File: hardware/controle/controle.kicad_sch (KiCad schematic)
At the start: 44 parts, among them J3 PWR, J4 DATA, J5 UART7, J6 TWI3, J7 SENS0375, J8 TWI4, J9 LED, U2 MCP7940N-xSN, U4 ULN2003, Y1 32.768Khz

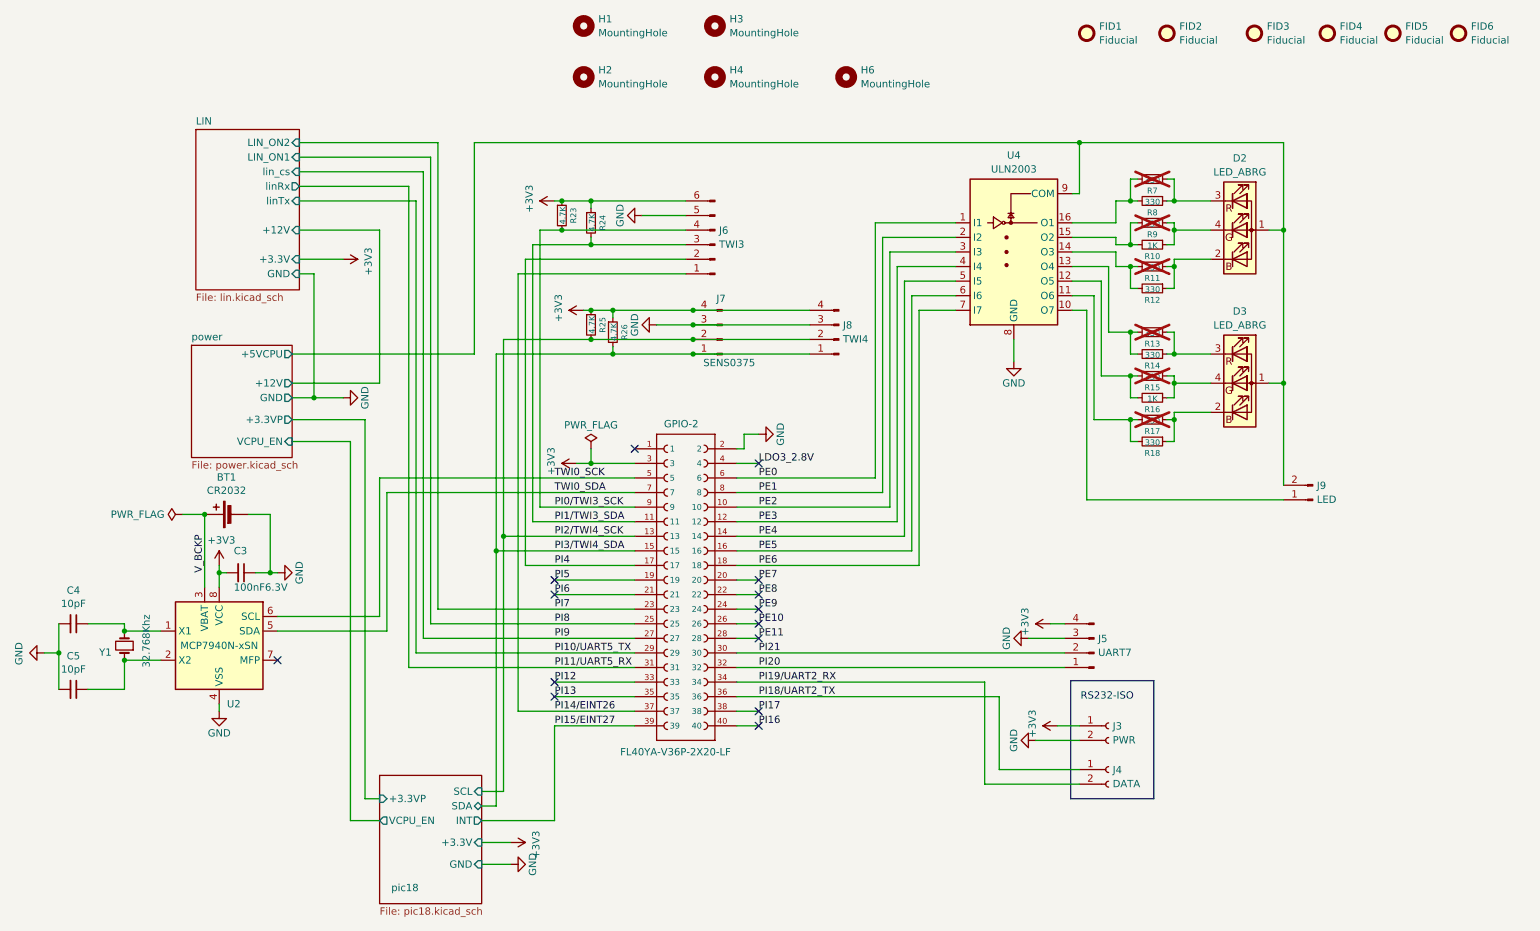
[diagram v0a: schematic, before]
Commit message: hardware/controle: route control CPU power from pic18
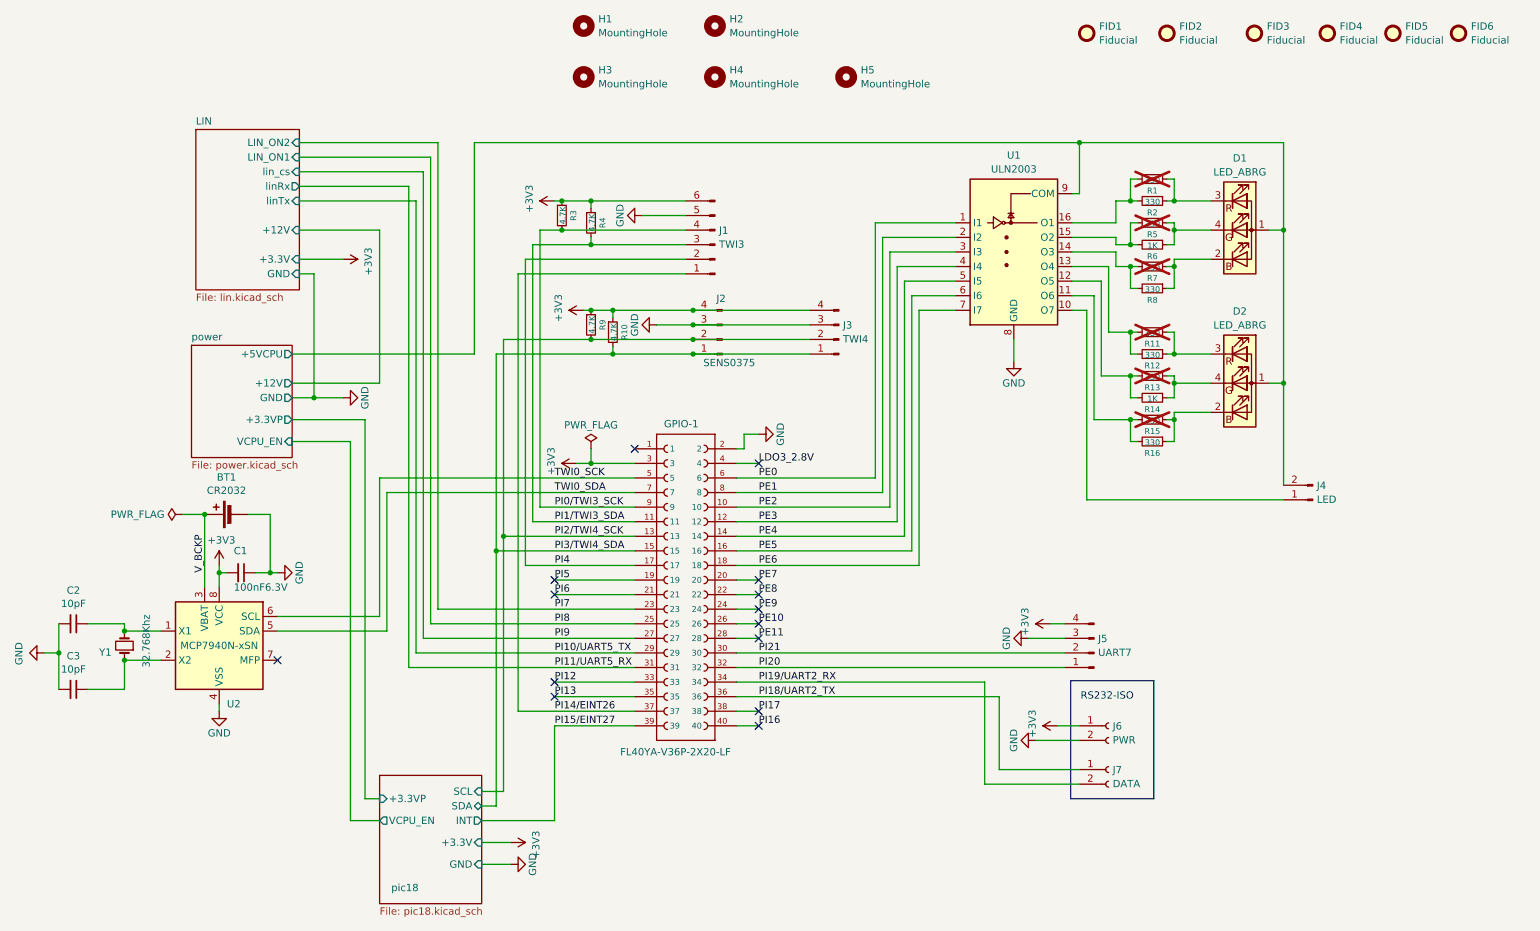
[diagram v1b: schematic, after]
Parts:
- renumbered C3 to C1, C4 to C2, C5 to C3, D2 to D1, D3 to D2, GPIO-2 to GPIO-1, H3 to H2, H2 to H3, H6 to H5, J6 to J1, J7 to J2, J8 to J3, J9 to J4, J3 to J6, J4 to J7, R7 to R1, R26 to R10, R13 to R11, R14 to R12, R15 to R13, R16 to R14, R17 to R15, R18 to R16, R8 to R2, R23 to R3, R24 to R4, R9 to R5, R10 to R6, R11 to R7, R12 to R8, R25 to R9, U4 to U1

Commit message: hardware/controle: update some component values and P/N
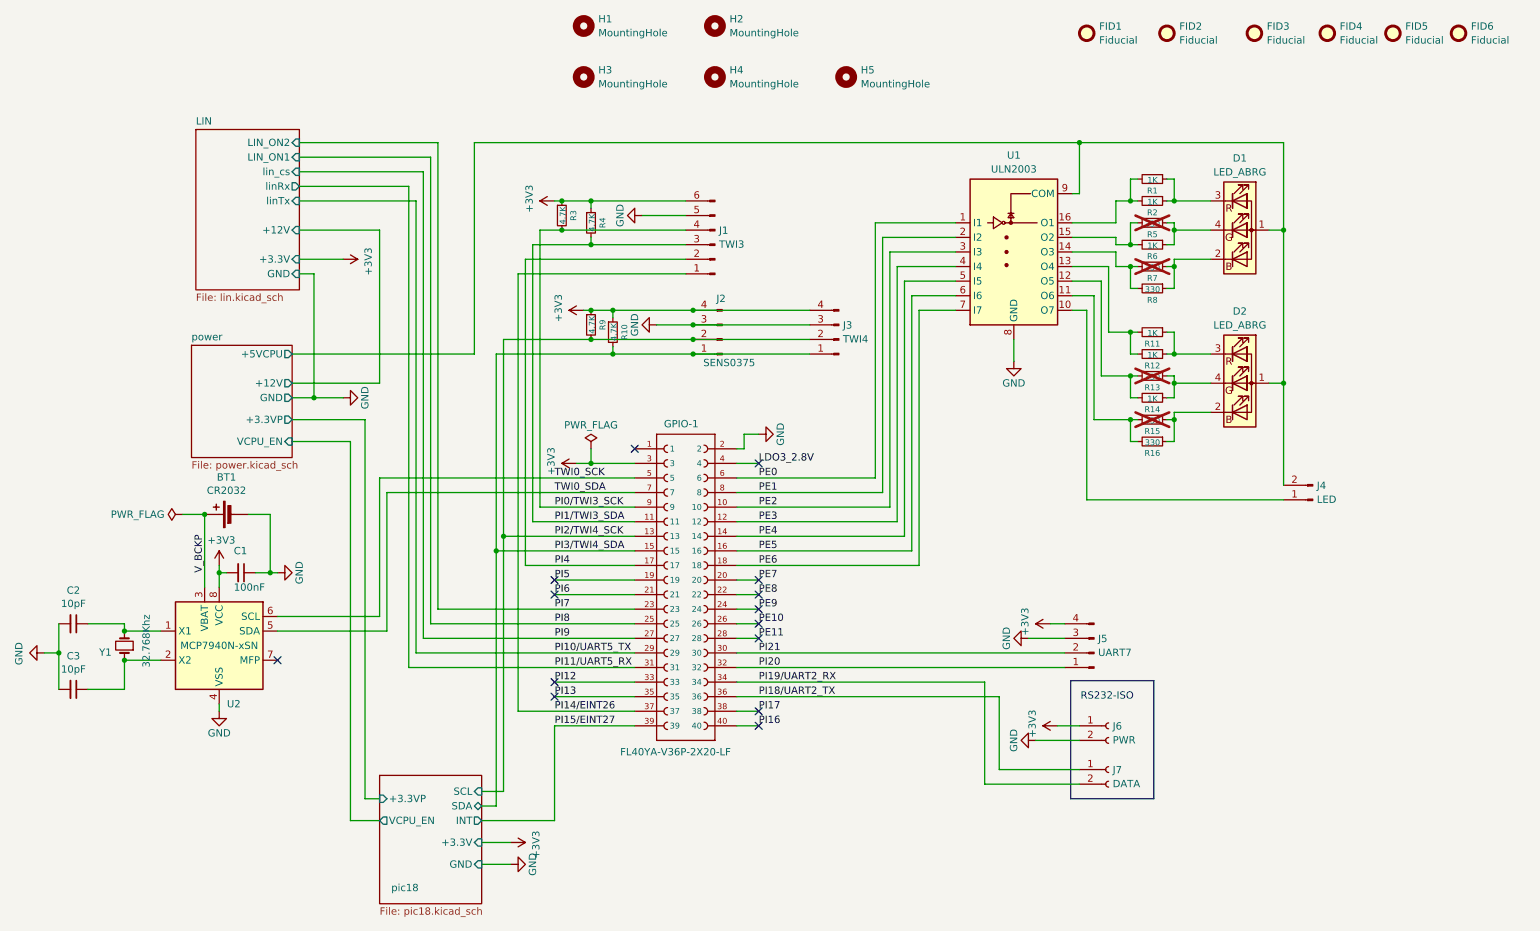
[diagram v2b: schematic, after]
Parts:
- C1: value 100nF6.3V -> 100nF; P/N stock -> CC0805KKX7RYBB104
- R1, R11: value 330 -> 1K; P/N stock -> MCWR08X1001FTL; now fitted
- R10, R3, R4, R9: P/N stock -> MCWR08X4701FTL
- R12, R2: value 330 -> 1K; P/N stock -> MCWR08X1001FTL
- R13, R15, R16, R5, R7, R8: P/N stock -> MCWR08X3300FTL
- R14, R6: P/N stock -> MCWR08X1001FTL
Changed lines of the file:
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@@
 			)
 		)
-		(property "P/N" "stock"
+		(property "P/N" "MCWR08X3300FTL"
 			(at 217.17 59.69 0)
 			(effects
@@
 			)
 		)
-		(property "Value" "330"
+		(property "Value" "1K"
 			(at 217.1954 75.1078 90)
 			(effects
@@
 			)
 		)
-		(property "P/N" "stock"
+		(property "P/N" "MCWR08X1001FTL"
 			(at 217.17 74.93 0)
 			(effects
@@
 		(in_bom yes)
 		(on_board yes)
-		(dnp yes)
+		(dnp no)
 		(property "Reference" "R1"
 			(at 217.17 46.482 90)
@@
 			)
 		)
-		(property "Value" "330"
+		(property "Value" "1K"
 			(at 217.1954 44.6278 90)
 			(effects
@@
 			)
 		)
-		(property "P/N" "stock"
+		(property "P/N" "MCWR08X1001FTL"
 			(at 217.17 44.45 0)
 			(effects
@@
 			)
 		)
-		(property "P/N" "stock"
+		(property "P/N" "MCWR08X4701FTL"
 			(at 123.19 71.12 0)
 			(effects
@@
 			)
 		)
-		(property "P/N" "stock"
+		(property "P/N" "MCWR08X1001FTL"
 			(at 217.17 82.55 0)
 			(effects
@@
 			)
 		)
-		(property "P/N" "stock"
+		(property "P/N" "MCWR08X3300FTL"
 			(at 217.17 52.07 0)
 			(effects
@@
 			)
 		)
-		(property "P/N" "stock"
+		(property "P/N" "MCWR08X4701FTL"
 			(at 119.38 69.85 0)
 			(effects
@@
 			)
 		)
-		(property "P/N" "stock"
+		(property "P/N" "MCWR08X4701FTL"
 			(at 114.3 50.8 0)
 			(effects
@@
 			)
 		)
-		(property "P/N" "stock"
+		(property "P/N" "MCWR08X1001FTL"
 			(at 217.17 55.88 0)
 			(effects
@@
 			)
 		)
-		(property "P/N" "stock"
+		(property "P/N" "MCWR08X3300FTL"
 			(at 217.17 90.17 0)
 			(effects
@@
 		(in_bom yes)
 		(on_board yes)
-		(dnp yes)
+		(dnp no)
 		(property "Reference" "R11"
 			(at 217.17 73.152 90)
@@
 			)
 		)
-		(property "Value" "330"
+		(property "Value" "1K"
 			(at 217.1954 71.2978 90)
 			(effects
@@
 			)
 		)
-		(property "P/N" "stock"
+		(property "P/N" "MCWR08X1001FTL"
 			(at 217.17 71.12 0)
 			(effects
@@
 			)
 		)
-		(property "P/N" "stock"
+		(property "P/N" "MCWR08X4701FTL"
 			(at 119.38 52.07 0)
 			(effects
@@
 			)
 		)
-		(property "P/N" "stock"
+		(property "P/N" "MCWR08X3300FTL"
 			(at 217.17 78.74 0)
 			(effects
@@
 			)
 		)
-		(property "Value" "100nF6.3V"
+		(property "Value" "100nF"
 			(at 57.15 115.57 90)
 			(effects
@@
 			)
 		)
-		(property "P/N" "stock"
+		(property "P/N" "CC0805KKX7RYBB104"
 			(at 90.17 63.5 0)
 			(effects
@@
 			)
 		)
-		(property "P/N" "stock"
+		(property "P/N" "MCWR08X3300FTL"
 			(at 217.17 63.5 0)
 			(effects
@@
 			)
 		)
-		(property "Value" "330"
+		(property "Value" "1K"
 			(at 217.1954 48.4378 90)
 			(effects
@@
 			)
 		)
-		(property "P/N" "stock"
+		(property "P/N" "MCWR08X1001FTL"
 			(at 217.17 48.26 0)
 			(effects
@@
 			)
 		)
-		(property "P/N" "stock"
+		(property "P/N" "MCWR08X3300FTL"
 			(at 217.17 86.36 0)
 			(effects

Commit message: hardware/controle: update P/N of 100nF capacitors
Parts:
- C1: P/N CC0805KKX7RYBB104 -> C0603C104K5RAC7411
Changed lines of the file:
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@@
 			)
 		)
-		(property "P/N" "CC0805KKX7RYBB104"
+		(property "P/N" "C0603C104K5RAC7411"
 			(at 90.17 63.5 0)
 			(effects
